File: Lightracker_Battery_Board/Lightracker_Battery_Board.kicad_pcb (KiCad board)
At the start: 2 copper layers, 56 x 80 mm, 8 parts, among them J1 B2B-XH-A, J2 Conn_02x08_Odd_Even, J3 Conn_02x08_Odd_Even, U1 DF Robot DC-DC Converter, U2 Light Tracker Lora APRS Unit

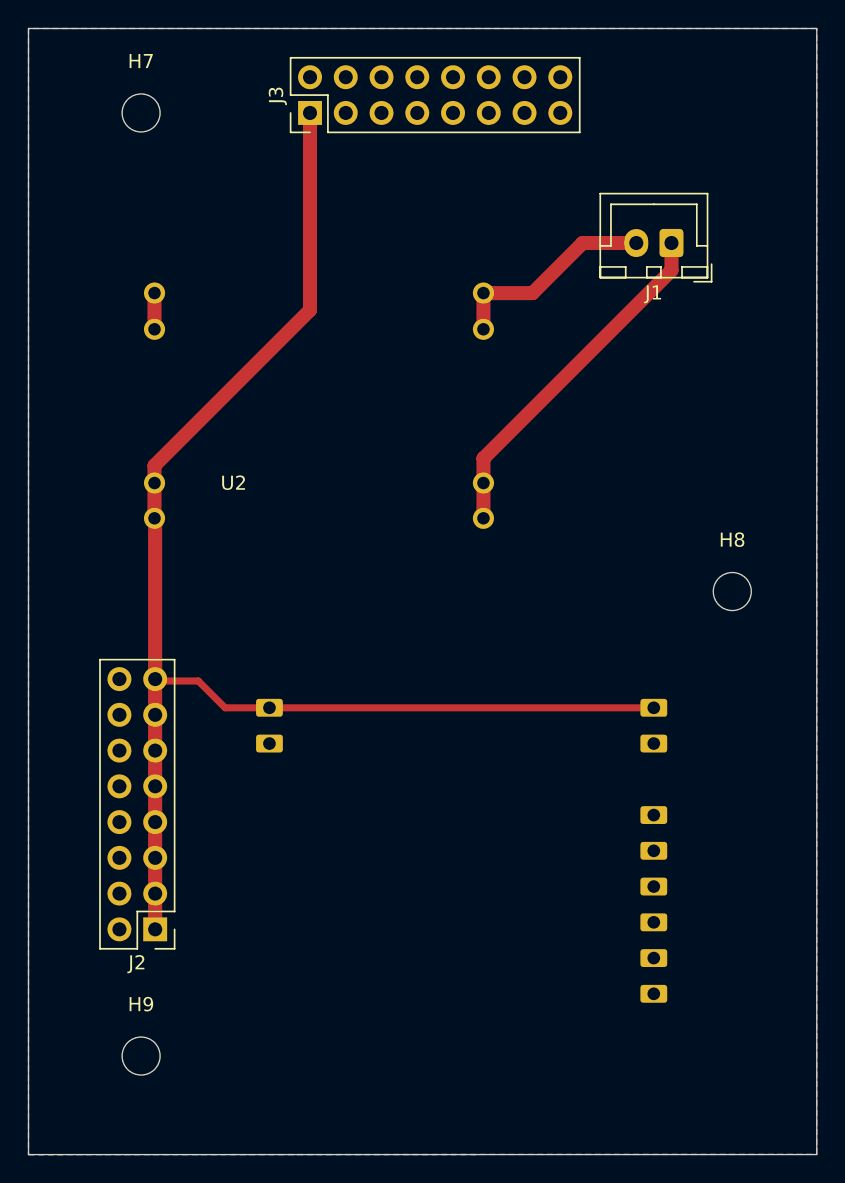
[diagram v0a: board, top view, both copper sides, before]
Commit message: Fix flipped components
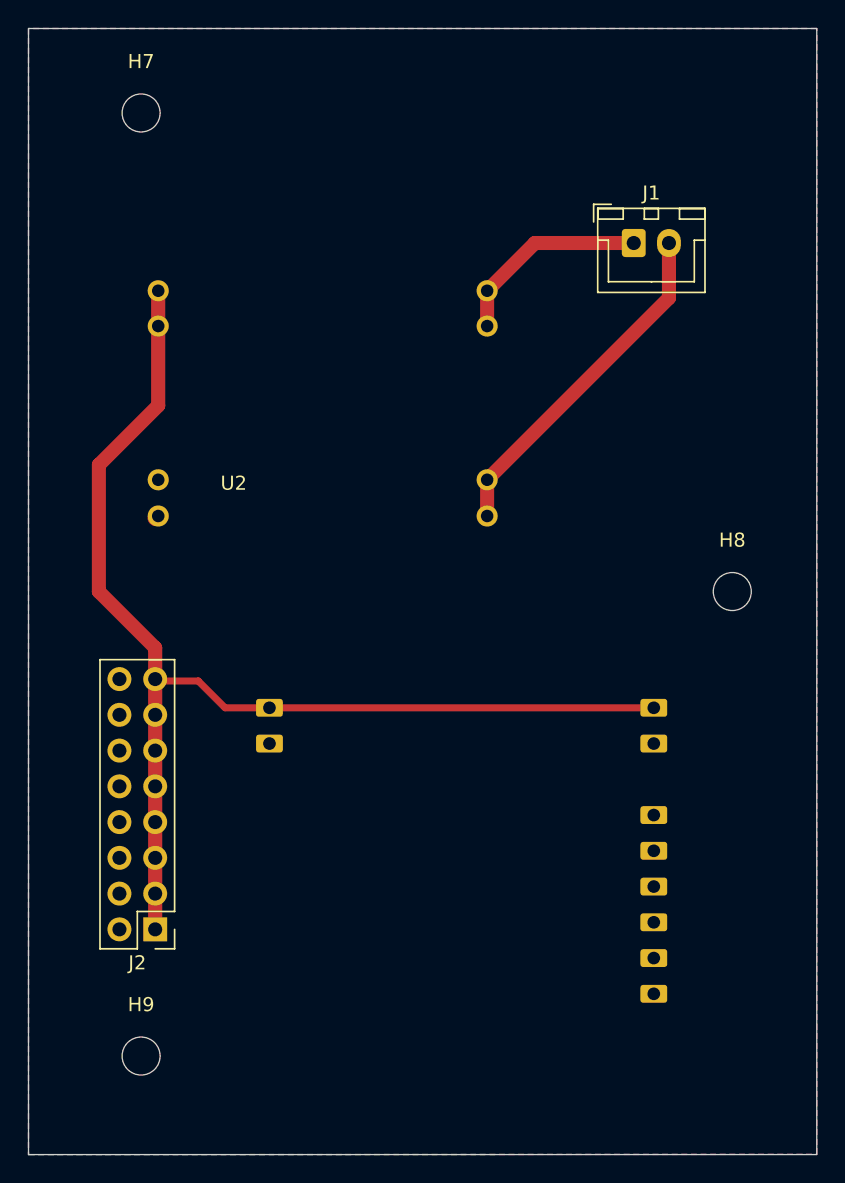
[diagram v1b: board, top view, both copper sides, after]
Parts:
- removed J3: Conn_02x08_Odd_Even, Connector_PinHeader_2.54mm:PinHeader_2x08_P2.54mm_Vertical
- U1: moved to B.Cu
- moved U1 20.2 mm to (64.6, 46.6)
- moved J1 2.68 mm to (73.0, 45.2), turned to 0 degrees
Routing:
- net /+5V: track 98.9 -> 85.0 mm
- net /+7V4: track 25.1 -> 14.3 mm
- net Net-(U1-GND_IN): track 14.9 -> 24.7 mm
- net /Board_2_GND: track 2.57 -> 0.07 mm
